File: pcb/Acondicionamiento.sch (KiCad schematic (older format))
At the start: 6 parts, among them U5 LM2903

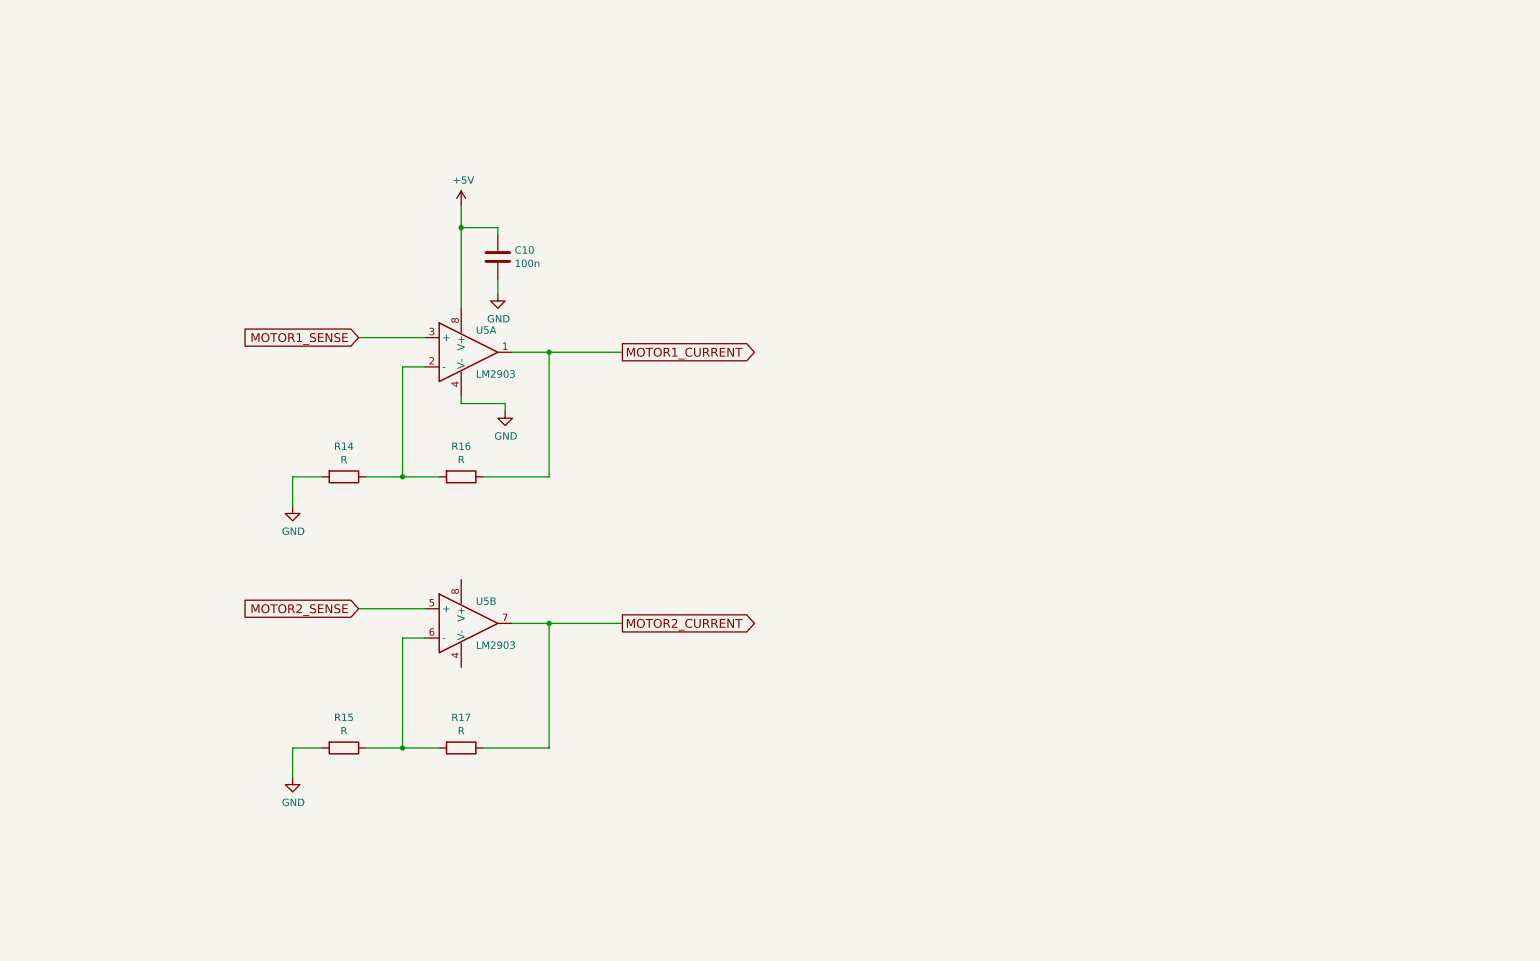
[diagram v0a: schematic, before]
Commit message: finalizada realizacion de esquema
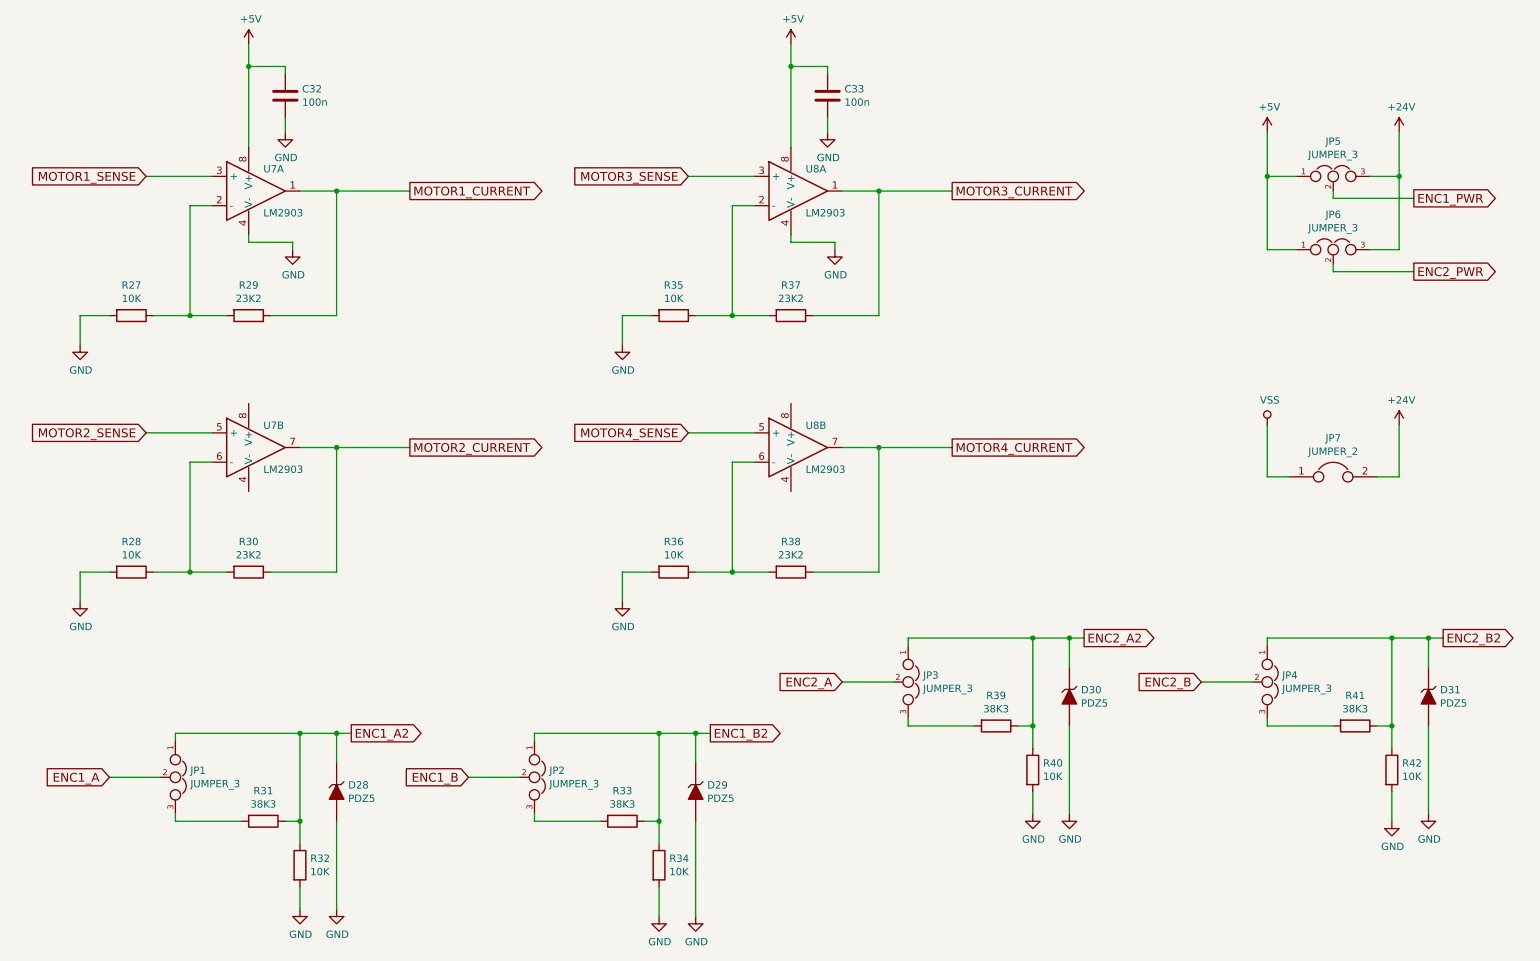
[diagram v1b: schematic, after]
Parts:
- added C33: 100n, symbol C
- added D28, D29, D30, D31: PDZ5, symbol ZENER
- added JP1, JP2, JP3, JP4, JP5, JP6: JUMPER_3, symbol JUMPER_3
- added JP7: JUMPER_2, symbol JUMPER_2
- added R31, R33, R39, R41: 38K3, symbol R
- added R32, R34, R35, R36, R40, R42: 10K, symbol R
- added R37, R38: 23K2, symbol R
- added U8: LM2903, symbol D_OPAM
- R27: renamed from R14; value R -> 10K; Fabricante (none) -> vishay; Potencia (none) -> 0.125W; Provedor (none) -> tme; Ref (none) -> CRCW080510K0FKEA; Ref_Proveedor (none) -> CRCW080510K0FKEA; Tolerancia (none) -> 1%
- R28: renamed from R15; value R -> 10K; Fabricante (none) -> vishay; Potencia (none) -> 0.125W; Provedor (none) -> tme; Ref (none) -> CRCW080510K0FKEA; Ref_Proveedor (none) -> CRCW080510K0FKEA; Tolerancia (none) -> 1%
- R29: renamed from R16; value R -> 23K2; Fabricante (none) -> VISHAY; Provedor (none) -> tme; Ref (none) -> CRCW080523K2FKTABC; Ref_Proveedor (none) -> CRCW080523K2FKTABC
- R30: renamed from R17; value R -> 23K2; Fabricante (none) -> VISHAY; Provedor (none) -> tme; Ref (none) -> CRCW080523K2FKTABC; Ref_Proveedor (none) -> CRCW080523K2FKTABC
- renumbered C10 to C32, U5 to U7
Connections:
- net +5V: now also C33.1, JP5.1, JP6.1, U8.8 (V+)
- net GND: now also C33.2, D28.2 (A), D29.2 (A), D30.2 (A), D31.2 (A), R32.2, R34.2, R35.2, R36.2, R40.2, R42.2, U8.4 (V-)
- new net: R35.1, R37.2, U8.2 (-)
- new net: R36.1, R38.2, U8.6 (-)
- new net: JP1.3, R31.2
- new net: JP2.3, R33.2
- new net: JP3.3, R39.2
- new net: JP4.3, R41.2
- new net +24V: JP5.3, JP6.3, JP7.2
- new net ENC1_A: JP1.2
- new net ENC1_A2: D28.1 (K), JP1.1, R31.1, R32.1
- new net ENC1_B: JP2.2
- new net ENC1_B2: D29.1 (K), JP2.1, R33.1, R34.1
- new net ENC1_PWR: JP5.2
- new net ENC2_A: JP3.2
- new net ENC2_A2: D30.1 (K), JP3.1, R39.1, R40.1
- new net ENC2_B: JP4.2
- new net ENC2_B2: D31.1 (K), JP4.1, R41.1, R42.1
- new net ENC2_PWR: JP6.2
- new net MOTOR3_CURRENT: R37.1, U8.1
- new net MOTOR3_SENSE: U8.3 (+)
- new net MOTOR4_CURRENT: R38.1, U8.7
- new net MOTOR4_SENSE: U8.5 (+)
- new net VSS: JP7.1
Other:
- moved on the sheet: C32, R27, R28, R29, R30, U7A, U7B

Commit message: asociacion de huellas a resistencias y condensadores
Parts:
- C32, C33: footprint (none) -> Capacitors_SMD:C_0805
- R27, R28, R29, R30, R31, R32, R33, R34, R35, R36, R37, R38, R39, R40, R41, R42: footprint (none) -> Resistors_SMD:R_0805
- U7, U8: footprint (none) -> Housings_SOIC:SOIC-8_3.9x4.9mm_Pitch1.27mm
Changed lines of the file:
@@
 F 0 "U7" H 2400 2050 50  0000 L CNN
 F 1 "LM2903" H 2400 1750 50  0000 L CNN
-F 2 "" H 2360 1900 50  0000 C CNN
+F 2 "Housings_SOIC:SOIC-8_3.9x4.9mm_Pitch1.27mm" H 2360 1900 50  0001 C CNN
 F 3 "" H 2360 1900 50  0000 C CNN
 F 4 "ti" H 2300 1900 60  0001 C CNN "Fabricante"
@@
 F 0 "R29" V 2093 2750 50  0000 C CNN
 F 1 "23K2" V 2184 2750 50  0000 C CNN
-F 2 "" V 2230 2750 50  0000 C CNN
+F 2 "Resistors_SMD:R_0805" V 2230 2750 50  0001 C CNN
 F 3 "" H 2300 2750 50  0000 C CNN
 F 4 "VISHAY" H 2300 1900 60  0001 C CNN "Fabricante"
@@
 F 0 "R27" V 1293 2750 50  0000 C CNN
 F 1 "10K" V 1384 2750 50  0000 C CNN
-F 2 "" V 1430 2750 50  0000 C CNN
+F 2 "Resistors_SMD:R_0805" V 1430 2750 50  0001 C CNN
 F 3 "" H 1500 2750 50  0000 C CNN
 F 4 "vishay" H 1800 3700 60  0001 C CNN "Fabricante"
@@
 F 0 "R30" V 2093 4500 50  0000 C CNN
 F 1 "23K2" V 2184 4500 50  0000 C CNN
-F 2 "" V 2230 4500 50  0000 C CNN
+F 2 "Resistors_SMD:R_0805" V 2230 4500 50  0001 C CNN
 F 3 "" H 2300 4500 50  0000 C CNN
 F 4 "VISHAY" H 2300 1900 60  0001 C CNN "Fabricante"
@@
 F 0 "R28" V 1293 4500 50  0000 C CNN
 F 1 "10K" V 1384 4500 50  0000 C CNN
-F 2 "" V 1430 4500 50  0000 C CNN
+F 2 "Resistors_SMD:R_0805" V 1430 4500 50  0001 C CNN
 F 3 "" H 1500 4500 50  0000 C CNN
 F 4 "vishay" H 1800 3700 60  0001 C CNN "Fabricante"
@@
 F 0 "U7" H 2400 3800 50  0000 L CNN
 F 1 "LM2903" H 2400 3500 50  0000 L CNN
-F 2 "" H 2350 3650 50  0000 C CNN
+F 2 "Housings_SOIC:SOIC-8_3.9x4.9mm_Pitch1.27mm" H 2350 3650 50  0001 C CNN
 F 3 "" H 2350 3650 50  0000 C CNN
 F 4 "ti" H 2300 3650 60  0001 C CNN "Fabricante"
@@
 F 0 "C32" H 2665 1296 50  0000 L CNN
 F 1 "100n" H 2665 1205 50  0000 L CNN
-F 2 "" H 2588 1100 50  0000 C CNN
+F 2 "Capacitors_SMD:C_0805" H 2588 1100 50  0001 C CNN
 F 3 "" H 2550 1250 50  0000 C CNN
 F 4 "avx" H 2550 1250 60  0001 C CNN "Fabricante"
@@
 F 0 "U8" H 6100 2050 50  0000 L CNN
 F 1 "LM2903" H 6100 1750 50  0000 L CNN
-F 2 "" H 6060 1900 50  0000 C CNN
+F 2 "Housings_SOIC:SOIC-8_3.9x4.9mm_Pitch1.27mm" H 6060 1900 50  0001 C CNN
 F 3 "" H 6060 1900 50  0000 C CNN
 F 4 "ti" H 6000 1900 60  0001 C CNN "Fabricante"
@@
 F 0 "R37" V 5793 2750 50  0000 C CNN
 F 1 "23K2" V 5884 2750 50  0000 C CNN
-F 2 "" V 5930 2750 50  0000 C CNN
+F 2 "Resistors_SMD:R_0805" V 5930 2750 50  0001 C CNN
 F 3 "" H 6000 2750 50  0000 C CNN
 F 4 "VISHAY" H 2300 1900 60  0001 C CNN "Fabricante"
@@
 F 0 "R35" V 4993 2750 50  0000 C CNN
 F 1 "10K" V 5084 2750 50  0000 C CNN
-F 2 "" V 5130 2750 50  0000 C CNN
+F 2 "Resistors_SMD:R_0805" V 5130 2750 50  0001 C CNN
 F 3 "" H 5200 2750 50  0000 C CNN
 F 4 "vishay" H 1800 3700 60  0001 C CNN "Fabricante"
@@
 F 0 "R38" V 5793 4500 50  0000 C CNN
 F 1 "23K2" V 5884 4500 50  0000 C CNN
-F 2 "" V 5930 4500 50  0000 C CNN
+F 2 "Resistors_SMD:R_0805" V 5930 4500 50  0001 C CNN
 F 3 "" H 6000 4500 50  0000 C CNN
 F 4 "VISHAY" H 2300 1900 60  0001 C CNN "Fabricante"
@@
 F 0 "R36" V 4993 4500 50  0000 C CNN
 F 1 "10K" V 5084 4500 50  0000 C CNN
-F 2 "" V 5130 4500 50  0000 C CNN
+F 2 "Resistors_SMD:R_0805" V 5130 4500 50  0001 C CNN
 F 3 "" H 5200 4500 50  0000 C CNN
 F 4 "vishay" H 1800 3700 60  0001 C CNN "Fabricante"
@@
 F 0 "U8" H 6100 3800 50  0000 L CNN
 F 1 "LM2903" H 6100 3500 50  0000 L CNN
-F 2 "" H 6050 3650 50  0000 C CNN
+F 2 "Housings_SOIC:SOIC-8_3.9x4.9mm_Pitch1.27mm" H 6050 3650 50  0001 C CNN
 F 3 "" H 6050 3650 50  0000 C CNN
 F 4 "ti" H 6000 3650 60  0001 C CNN "Fabricante"
@@
 F 0 "C33" H 6365 1296 50  0000 L CNN
 F 1 "100n" H 6365 1205 50  0000 L CNN
-F 2 "" H 6288 1100 50  0000 C CNN
+F 2 "Capacitors_SMD:C_0805" H 6288 1100 50  0001 C CNN
 F 3 "" H 6250 1250 50  0000 C CNN
 F 4 "avx" H 6250 1250 60  0001 C CNN "Fabricante"
@@
 F 0 "JP5" H 9700 2039 50  0000 C CNN
 F 1 "JUMPER_3" H 9700 1948 50  0000 C CNN
-F 2 "" H 9700 1800 50  0000 C CNN
+F 2 "" H 9700 1800 50  0001 C CNN
 F 3 "" H 9700 1800 50  0000 C CNN
 F 4 "NINIGI" H 1800 5900 60  0001 C CNN "Fabricante"
@@
 F 0 "JP6" H 9700 2539 50  0000 C CNN
 F 1 "JUMPER_3" H 9700 2448 50  0000 C CNN
-F 2 "" H 9700 2300 50  0000 C CNN
+F 2 "" H 9700 2300 50  0001 C CNN
 F 3 "" H 9700 2300 50  0000 C CNN
 F 4 "NINIGI" H 1800 5900 60  0001 C CNN "Fabricante"
@@
 F 0 "JP1" V 1754 6002 50  0000 L CNN
 F 1 "JUMPER_3" V 1845 6002 50  0000 L CNN
-F 2 "" H 1800 5900 50  0000 C CNN
+F 2 "" H 1800 5900 50  0001 C CNN
 F 3 "" H 1800 5900 50  0000 C CNN
 F 4 "NINIGI" H 1800 5900 60  0001 C CNN "Fabricante"
@@
 F 0 "JP2" V 4204 6002 50  0000 L CNN
 F 1 "JUMPER_3" V 4295 6002 50  0000 L CNN
-F 2 "" H 4250 5900 50  0000 C CNN
+F 2 "" H 4250 5900 50  0001 C CNN
 F 3 "" H 4250 5900 50  0000 C CNN
 F 4 "NINIGI" H 1800 5900 60  0001 C CNN "Fabricante"
@@
 F 0 "R31" V 2193 6200 50  0000 C CNN
 F 1 "38K3" V 2284 6200 50  0000 C CNN
-F 2 "" V 2330 6200 50  0000 C CNN
+F 2 "Resistors_SMD:R_0805" V 2330 6200 50  0001 C CNN
 F 3 "" H 2400 6200 50  0000 C CNN
 F 4 "VISHAY" H 2300 1900 60  0001 C CNN "Fabricante"
@@
 F 0 "R33" V 4643 6200 50  0000 C CNN
 F 1 "38K3" V 4734 6200 50  0000 C CNN
-F 2 "" V 4780 6200 50  0000 C CNN
+F 2 "Resistors_SMD:R_0805" V 4780 6200 50  0001 C CNN
 F 3 "" H 4850 6200 50  0000 C CNN
 F 4 "VISHAY" H 2300 1900 60  0001 C CNN "Fabricante"
@@
 F 0 "R32" H 2720 6546 50  0000 L CNN
 F 1 "10K" H 2720 6455 50  0000 L CNN
-F 2 "" V 2580 6500 50  0000 C CNN
+F 2 "Resistors_SMD:R_0805" V 2580 6500 50  0001 C CNN
 F 3 "" H 2650 6500 50  0000 C CNN
 F 4 "vishay" H 1800 3700 60  0001 C CNN "Fabricante"
@@
 F 0 "R34" H 5170 6546 50  0000 L CNN
 F 1 "10K" H 5170 6455 50  0000 L CNN
-F 2 "" V 5030 6500 50  0000 C CNN
+F 2 "Resistors_SMD:R_0805" V 5030 6500 50  0001 C CNN
 F 3 "" H 5100 6500 50  0000 C CNN
 F 4 "vishay" H 1800 3700 60  0001 C CNN "Fabricante"
@@
 F 0 "JP3" V 6754 5352 50  0000 L CNN
 F 1 "JUMPER_3" V 6845 5352 50  0000 L CNN
-F 2 "" H 6800 5250 50  0000 C CNN
+F 2 "" H 6800 5250 50  0001 C CNN
 F 3 "" H 6800 5250 50  0000 C CNN
 F 4 "NINIGI" H 1800 5900 60  0001 C CNN "Fabricante"
@@
 F 0 "JP4" V 9204 5352 50  0000 L CNN
 F 1 "JUMPER_3" V 9295 5352 50  0000 L CNN
-F 2 "" H 9250 5250 50  0000 C CNN
+F 2 "" H 9250 5250 50  0001 C CNN
 F 3 "" H 9250 5250 50  0000 C CNN
 F 4 "NINIGI" H 1800 5900 60  0001 C CNN "Fabricante"
@@
 F 0 "R39" V 7193 5550 50  0000 C CNN
 F 1 "38K3" V 7284 5550 50  0000 C CNN
-F 2 "" V 7330 5550 50  0000 C CNN
+F 2 "Resistors_SMD:R_0805" V 7330 5550 50  0001 C CNN
 F 3 "" H 7400 5550 50  0000 C CNN
 F 4 "VISHAY" H 2300 1900 60  0001 C CNN "Fabricante"
@@
 F 0 "R41" V 9643 5550 50  0000 C CNN
 F 1 "38K3" V 9734 5550 50  0000 C CNN
-F 2 "" V 9780 5550 50  0000 C CNN
+F 2 "Resistors_SMD:R_0805" V 9780 5550 50  0001 C CNN
 F 3 "" H 9850 5550 50  0000 C CNN
 F 4 "VISHAY" H 2300 1900 60  0001 C CNN "Fabricante"
@@
 F 0 "R40" H 7720 5896 50  0000 L CNN
 F 1 "10K" H 7720 5805 50  0000 L CNN
-F 2 "" V 7580 5850 50  0000 C CNN
+F 2 "Resistors_SMD:R_0805" V 7580 5850 50  0001 C CNN
 F 3 "" H 7650 5850 50  0000 C CNN
 F 4 "vishay" H 1800 3700 60  0001 C CNN "Fabricante"
@@
 F 0 "R42" H 10170 5896 50  0000 L CNN
 F 1 "10K" H 10170 5805 50  0000 L CNN
-F 2 "" V 10030 5850 50  0000 C CNN
+F 2 "Resistors_SMD:R_0805" V 10030 5850 50  0001 C CNN
 F 3 "" H 10100 5850 50  0000 C CNN
 F 4 "vishay" H 1800 3700 60  0001 C CNN "Fabricante"
@@
 F 0 "D31" V 10304 5429 50  0000 L CNN
 F 1 "PDZ5" V 10395 5429 50  0000 L CNN
-F 2 "" H 10350 5350 50  0000 C CNN
+F 2 "" H 10350 5350 50  0001 C CNN
 F 3 "" H 10350 5350 50  0000 C CNN
 F 4 "NXP" H 1800 3700 60  0001 C CNN "Fabricante"
@@
 F 0 "D30" V 7854 5429 50  0000 L CNN
 F 1 "PDZ5" V 7945 5429 50  0000 L CNN
-F 2 "" H 7900 5350 50  0000 C CNN
+F 2 "" H 7900 5350 50  0001 C CNN
 F 3 "" H 7900 5350 50  0000 C CNN
 F 4 "NXP" H 1800 3700 60  0001 C CNN "Fabricante"
@@
 F 0 "D29" V 5304 6079 50  0000 L CNN
 F 1 "PDZ5" V 5395 6079 50  0000 L CNN
-F 2 "" H 5350 6000 50  0000 C CNN
+F 2 "" H 5350 6000 50  0001 C CNN
 F 3 "" H 5350 6000 50  0000 C CNN
 F 4 "NXP" H 1800 3700 60  0001 C CNN "Fabricante"
@@
 F 0 "D28" V 2854 6079 50  0000 L CNN
 F 1 "PDZ5" V 2945 6079 50  0000 L CNN
-F 2 "" H 2900 6000 50  0000 C CNN
+F 2 "" H 2900 6000 50  0001 C CNN
 F 3 "" H 2900 6000 50  0000 C CNN
 F 4 "NXP" H 1800 3700 60  0001 C CNN "Fabricante"
@@
 F 0 "JP7" H 9700 4114 50  0000 C CNN
 F 1 "JUMPER_2" H 9700 4023 50  0000 C CNN
-F 2 "" H 9700 3850 50  0000 C CNN
+F 2 "" H 9700 3850 50  0001 C CNN
 F 3 "" H 9700 3850 50  0000 C CNN
 F 4 "NINIGI" H 1800 5900 60  0001 C CNN "Fabricante"

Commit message: añadidas huellas para los borneros
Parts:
- D28, D29, D30, D31: footprint (none) -> Diodos:SOD-323
- JP1, JP2, JP3, JP4, JP5, JP6: footprint (none) -> Pin_Headers:Pin_Header_Straight_1x03
- JP7: footprint (none) -> Pin_Headers:Pin_Header_Straight_1x02
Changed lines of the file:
@@
 F 0 "JP5" H 9700 2039 50  0000 C CNN
 F 1 "JUMPER_3" H 9700 1948 50  0000 C CNN
-F 2 "" H 9700 1800 50  0001 C CNN
+F 2 "Pin_Headers:Pin_Header_Straight_1x03" H 9700 1800 50  0001 C CNN
 F 3 "" H 9700 1800 50  0000 C CNN
 F 4 "NINIGI" H 1800 5900 60  0001 C CNN "Fabricante"
@@
 F 0 "JP6" H 9700 2539 50  0000 C CNN
 F 1 "JUMPER_3" H 9700 2448 50  0000 C CNN
-F 2 "" H 9700 2300 50  0001 C CNN
+F 2 "Pin_Headers:Pin_Header_Straight_1x03" H 9700 2300 50  0001 C CNN
 F 3 "" H 9700 2300 50  0000 C CNN
 F 4 "NINIGI" H 1800 5900 60  0001 C CNN "Fabricante"
@@
 F 0 "JP1" V 1754 6002 50  0000 L CNN
 F 1 "JUMPER_3" V 1845 6002 50  0000 L CNN
-F 2 "" H 1800 5900 50  0001 C CNN
+F 2 "Pin_Headers:Pin_Header_Straight_1x03" H 1800 5900 50  0001 C CNN
 F 3 "" H 1800 5900 50  0000 C CNN
 F 4 "NINIGI" H 1800 5900 60  0001 C CNN "Fabricante"
@@
 F 0 "JP2" V 4204 6002 50  0000 L CNN
 F 1 "JUMPER_3" V 4295 6002 50  0000 L CNN
-F 2 "" H 4250 5900 50  0001 C CNN
+F 2 "Pin_Headers:Pin_Header_Straight_1x03" H 4250 5900 50  0001 C CNN
 F 3 "" H 4250 5900 50  0000 C CNN
 F 4 "NINIGI" H 1800 5900 60  0001 C CNN "Fabricante"
@@
 F 0 "JP3" V 6754 5352 50  0000 L CNN
 F 1 "JUMPER_3" V 6845 5352 50  0000 L CNN
-F 2 "" H 6800 5250 50  0001 C CNN
+F 2 "Pin_Headers:Pin_Header_Straight_1x03" H 6800 5250 50  0001 C CNN
 F 3 "" H 6800 5250 50  0000 C CNN
 F 4 "NINIGI" H 1800 5900 60  0001 C CNN "Fabricante"
@@
 F 0 "JP4" V 9204 5352 50  0000 L CNN
 F 1 "JUMPER_3" V 9295 5352 50  0000 L CNN
-F 2 "" H 9250 5250 50  0001 C CNN
+F 2 "Pin_Headers:Pin_Header_Straight_1x03" H 9250 5250 50  0001 C CNN
 F 3 "" H 9250 5250 50  0000 C CNN
 F 4 "NINIGI" H 1800 5900 60  0001 C CNN "Fabricante"
@@
 F 0 "D31" V 10304 5429 50  0000 L CNN
 F 1 "PDZ5" V 10395 5429 50  0000 L CNN
-F 2 "" H 10350 5350 50  0001 C CNN
+F 2 "Diodos:SOD-323" H 10350 5350 50  0001 C CNN
 F 3 "" H 10350 5350 50  0000 C CNN
 F 4 "NXP" H 1800 3700 60  0001 C CNN "Fabricante"
@@
 F 0 "D30" V 7854 5429 50  0000 L CNN
 F 1 "PDZ5" V 7945 5429 50  0000 L CNN
-F 2 "" H 7900 5350 50  0001 C CNN
+F 2 "Diodos:SOD-323" H 7900 5350 50  0001 C CNN
 F 3 "" H 7900 5350 50  0000 C CNN
 F 4 "NXP" H 1800 3700 60  0001 C CNN "Fabricante"
@@
 F 0 "D29" V 5304 6079 50  0000 L CNN
 F 1 "PDZ5" V 5395 6079 50  0000 L CNN
-F 2 "" H 5350 6000 50  0001 C CNN
+F 2 "Diodos:SOD-323" H 5350 6000 50  0001 C CNN
 F 3 "" H 5350 6000 50  0000 C CNN
 F 4 "NXP" H 1800 3700 60  0001 C CNN "Fabricante"
@@
 F 0 "D28" V 2854 6079 50  0000 L CNN
 F 1 "PDZ5" V 2945 6079 50  0000 L CNN
-F 2 "" H 2900 6000 50  0001 C CNN
+F 2 "Diodos:SOD-323" H 2900 6000 50  0001 C CNN
 F 3 "" H 2900 6000 50  0000 C CNN
 F 4 "NXP" H 1800 3700 60  0001 C CNN "Fabricante"
@@
 F 0 "JP7" H 9700 4114 50  0000 C CNN
 F 1 "JUMPER_2" H 9700 4023 50  0000 C CNN
-F 2 "" H 9700 3850 50  0001 C CNN
+F 2 "Pin_Headers:Pin_Header_Straight_1x02" H 9700 3850 50  0001 C CNN
 F 3 "" H 9700 3850 50  0000 C CNN
 F 4 "NINIGI" H 1800 5900 60  0001 C CNN "Fabricante"
